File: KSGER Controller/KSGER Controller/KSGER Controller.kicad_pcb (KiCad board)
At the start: 2 copper layers, 114.3 x 40.6 mm, 49 parts, among them J1 24 VDC, J2 IRON_IN, J4 BATT, J5 SWD, Q1 IRF7416, Q2 S8050, SW1 ENCODER, U1 STM32F103C8Tx, U2 AMS1117-3.3, U3 SGM8551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

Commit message: Moar board work
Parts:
- SW1, U7: moved to B.Cu
- moved R19 135.1 mm to (97.8, 97.8)
- moved C11 114.4 mm to (100.3, 104.1)
- moved J4 110.8 mm to (102.9, 114.3)
- moved R13 105.1 mm to (127.0, 105.4)
- moved SW1 104.5 mm to (100.3, 106.7), turned to 90 degrees
- moved R10 92.5 mm to (97.8, 95.2)
- moved U2 90.2 mm to (151.1, 109.2), turned to -90 degrees
- moved C4 87.4 mm to (131.1, 90.2)
- moved R16 86.1 mm to (184.2, 109.2)
- moved Y1 84.8 mm to (110.5, 94.0), turned to 90 degrees
- moved BZ1 84.6 mm to (113.0, 114.3)
- moved Q1 83.1 mm to (174.0, 106.7)
- moved R6 82.8 mm to (140.0, 105.4)
- moved J5 81.1 mm to (101.7, 81.3)
- moved U4 80.5 mm to (137.2, 95.2), turned to 90 degrees
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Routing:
- added copper zone on B.Cu, net GND
- added copper zone on F.Cu, net GND

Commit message: Added C5 and C6 from flobbydusts schematic
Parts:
- added C5: 0.1, Capacitor_SMD:C_0805_2012Metric, F.Cu at (135.6, 115.6)
- added C6: 0.1, Capacitor_SMD:C_0805_2012Metric, F.Cu at (131.5, 115.6)
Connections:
- D2 pad 2: Net-(D2-Pad2) -> +24V
- J1 pad 2: Net-(D2-Pad2) -> +24V
- R8 pad 2: Net-(D2-Pad2) -> +24V
- SW1 pad MP: (no net) -> GND

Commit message: Updated C10 and C11 to 1nF
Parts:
- C10, C11: value 0.1 -> 0.001
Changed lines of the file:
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@@
     (descr "Capacitor SMD 0805 (2012 Metric), square (rectangular) end terminal, IPC_7351 nominal, (Body size source: IPC-SM-782 page 76, https://www.pcb-3d.com/wordpress/wp-content/uploads/ipc-sm-782a_amendment_1_and_2.pdf, https://docs.google.com/spreadsheets/d/1BsfQQcO9C6DZCsRaXUlFlo91Tg2WpOkGARC1WS5S8t0/edit?usp=sharing), generated with kicad-footprint-generator")
     (tags "capacitor")
-    (property "JCLPCB Part #" "C49678")
+    (property "JCLPCB Part #" "C46653")
     (property "Sheetfile" "KSGER Controller.kicad_sch")
     (property "Sheetname" "")
@@
       (effects (font (size 1 1) (thickness 0.15)))
     )
-    (fp_text value "0.1" (at 0 1.68) (layer "F.Fab")
+    (fp_text value "0.001" (at 0 1.68) (layer "F.Fab")
       (effects (font (size 1 1) (thickness 0.15)))
     )
@@
     (descr "Capacitor SMD 0805 (2012 Metric), square (rectangular) end terminal, IPC_7351 nominal, (Body size source: IPC-SM-782 page 76, https://www.pcb-3d.com/wordpress/wp-content/uploads/ipc-sm-782a_amendment_1_and_2.pdf, https://docs.google.com/spreadsheets/d/1BsfQQcO9C6DZCsRaXUlFlo91Tg2WpOkGARC1WS5S8t0/edit?usp=sharing), generated with kicad-footprint-generator")
     (tags "capacitor")
-    (property "JCLPCB Part #" "C49678")
+    (property "JCLPCB Part #" "C46653")
     (property "Sheetfile" "KSGER Controller.kicad_sch")
     (property "Sheetname" "")
@@
       (effects (font (size 1 1) (thickness 0.15)))
     )
-    (fp_text value "0.1" (at 0 1.68) (layer "F.Fab")
-      (effects (font (size 1 1) (thickness 0.15)))
-    )
+    (fp_text value "0.001" (at 0 1.68) (layer "F.Fab")
+      (effects (font (size 1 1) (thickness 0.15)))
+    )

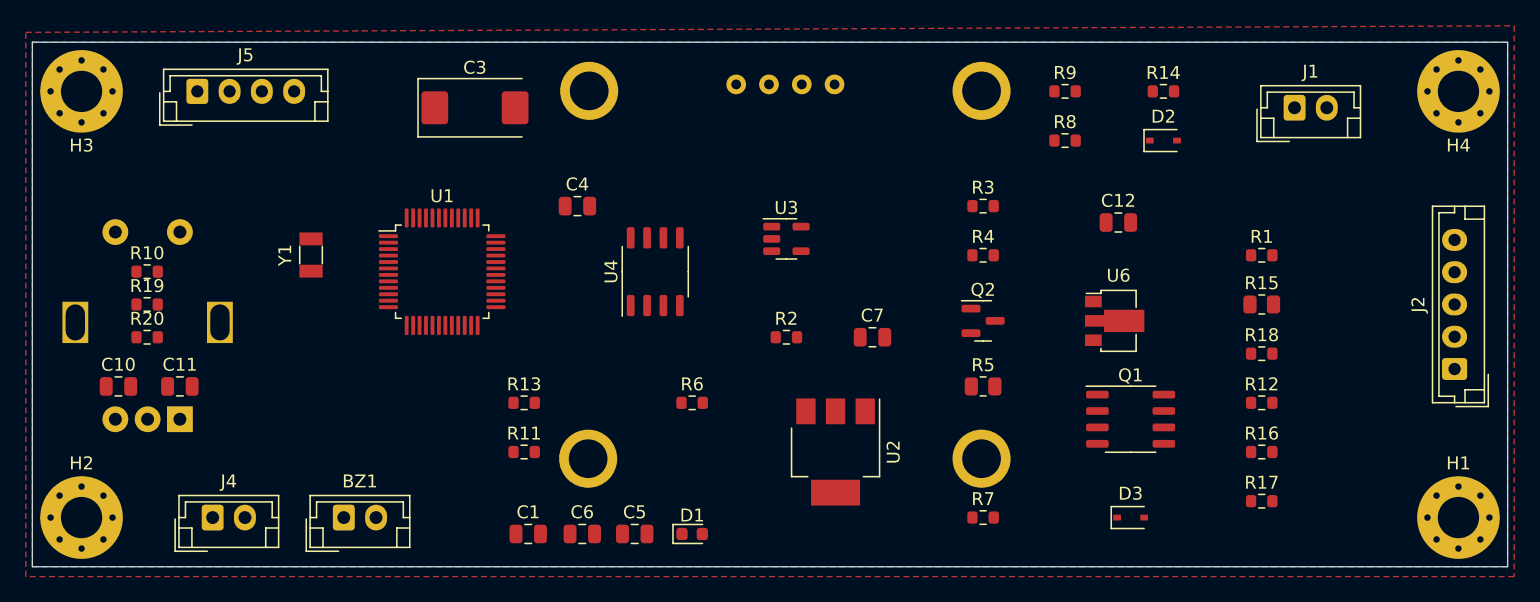
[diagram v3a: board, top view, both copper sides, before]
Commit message: Finished traces on board
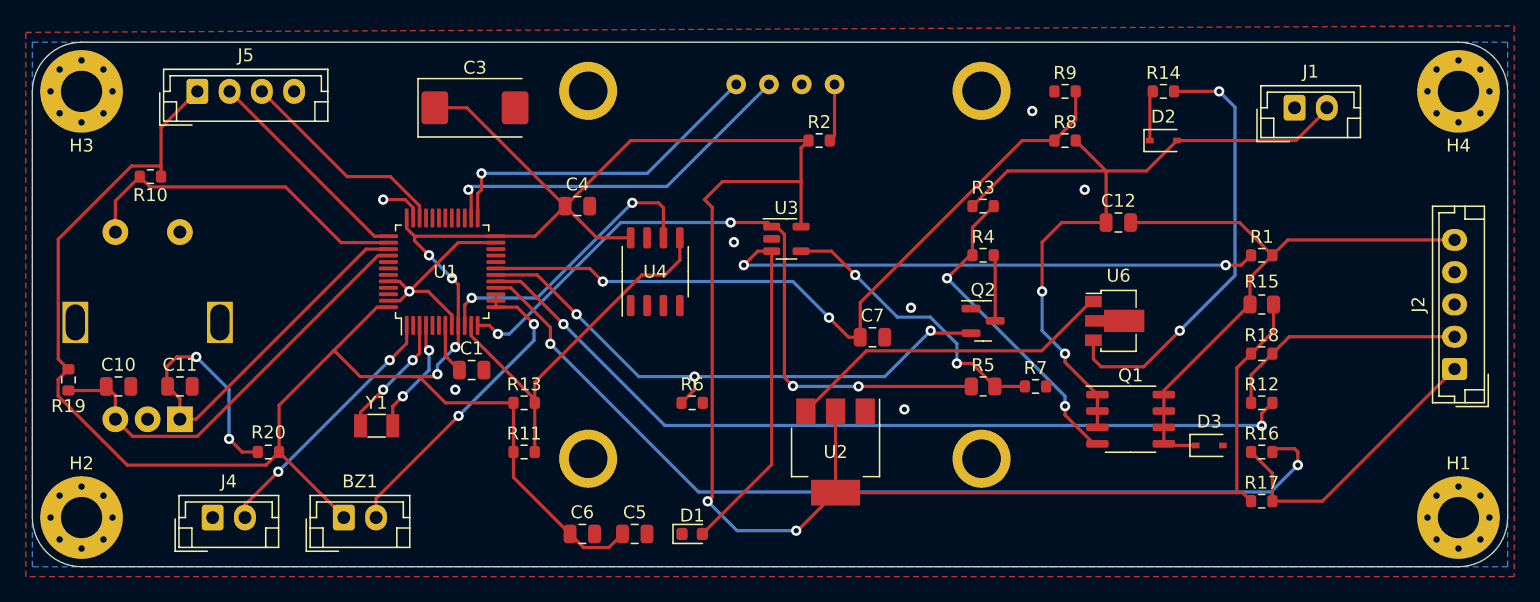
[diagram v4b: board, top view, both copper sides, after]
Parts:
- moved R2 15.5 mm to (149.9, 85.1)
- moved Y1 14.2 mm to (115.6, 107.2), turned to 180 degrees
- moved C1 13.4 mm to (122.9, 102.9)
- moved R20 12.9 mm to (107.2, 109.2), turned to 180 degrees
- moved R7 10.9 mm to (166.6, 104.1)
- moved R19 8.44 mm to (91.7, 103.6), turned to -90 degrees
- moved D3 8.27 mm to (180.1, 108.7)
- moved R10 7.37 mm to (98.0, 87.9), turned to 180 degrees
- turned R15 to 180 degrees
- turned U1 to 90 degrees
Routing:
- net +3V3: track 0.00 -> 280.5 mm, vias 0 -> 6
- net SHAKE: track 0.00 -> 73.5 mm, vias 0 -> 2
- net Net-(D1-Pad2): track 0.00 -> 66.4 mm, vias 0 -> 2
- net NTC: track 0.00 -> 66.1 mm, vias 0 -> 2
- net +24V: track 0.00 -> 59.7 mm, vias 0 -> 2
- net VIN_MON: track 0.00 -> 57.9 mm, vias 0 -> 2
- net TIP_TEMP: track 0.00 -> 53.9 mm, vias 0 -> 4
- net Net-(C12-Pad2): track 0.00 -> 47.3 mm
- net HEATER_ON: track 0.00 -> 44.1 mm, vias 0 -> 3
- net ENCODER_A: track 0.00 -> 38.7 mm, vias 0 -> 2
- net Net-(R14-Pad2): track 0.00 -> 33.9 mm, vias 0 -> 2
- net ENCODER_B: track 0.00 -> 33.4 mm
- net EE_SDA: track 0.00 -> 30.3 mm
- net OLED_SCL: track 0.00 -> 28.9 mm, vias 0 -> 1
- net ENCODER_SW: track 0.00 -> 26.5 mm
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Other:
- outline, holes or cut-outs redrawn

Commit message: Final touches to board layout
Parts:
- moved J2 5.84 mm to (193.2, 102.8)
- moved R2 2.75 mm to (151.4, 87.4)
- renumbered J5 to JE
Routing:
- net +3V3: track 280.5 -> 274.2 mm
- net Net-(J2-Pad2): track 19.2 -> 13.3 mm
- net Net-(C12-Pad2): track 47.3 -> 41.4 mm
- net Net-(R2-Pad2): track 4.50 -> 7.12 mm
- net Net-(J2-Pad1): track 22.8 -> 20.4 mm
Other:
- board text added: "+"
- board text added: "24 VDC"
- board text added: "BATTERY"
- board text added: "CLK"
- board text added: "E"
- board text added: "G"
- board text added: "GND"
- board text added: "IO"
- board text added: "N"
- board text added: "S"
- board text added: "SCL"
- board text added: "SDA"
- board text added: "SOLDERING IRON"
- board text added: "SPKR"
- board text added: "SWD"
- board text added: "T12 SOLDERING IRON CONTROL BOARD DESIGNED BY OMEGA9380 BASED ON SCHEMATICS BY MINDSTORM88"
- board text added: "VCC"
